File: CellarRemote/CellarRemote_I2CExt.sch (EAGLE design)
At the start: 14 parts, among them M1 BSS84, U1 P82B715D

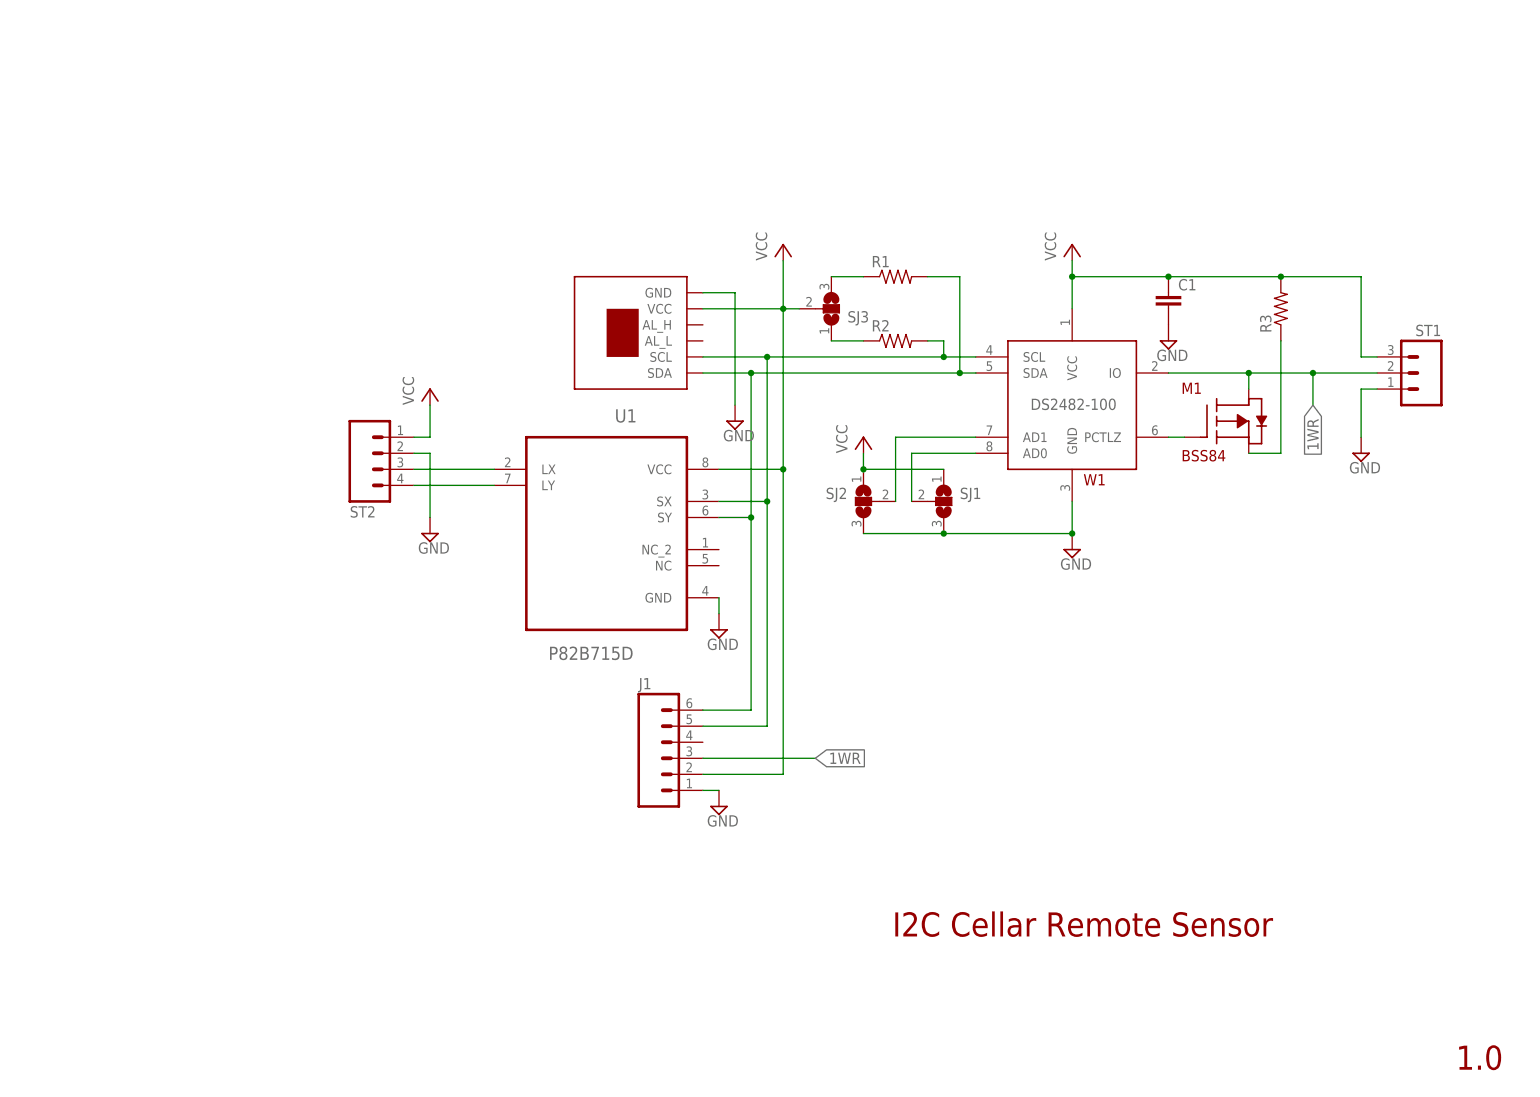
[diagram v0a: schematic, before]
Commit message: Added Raspberry pi board, updated I2C extender pullup resistors to other boards
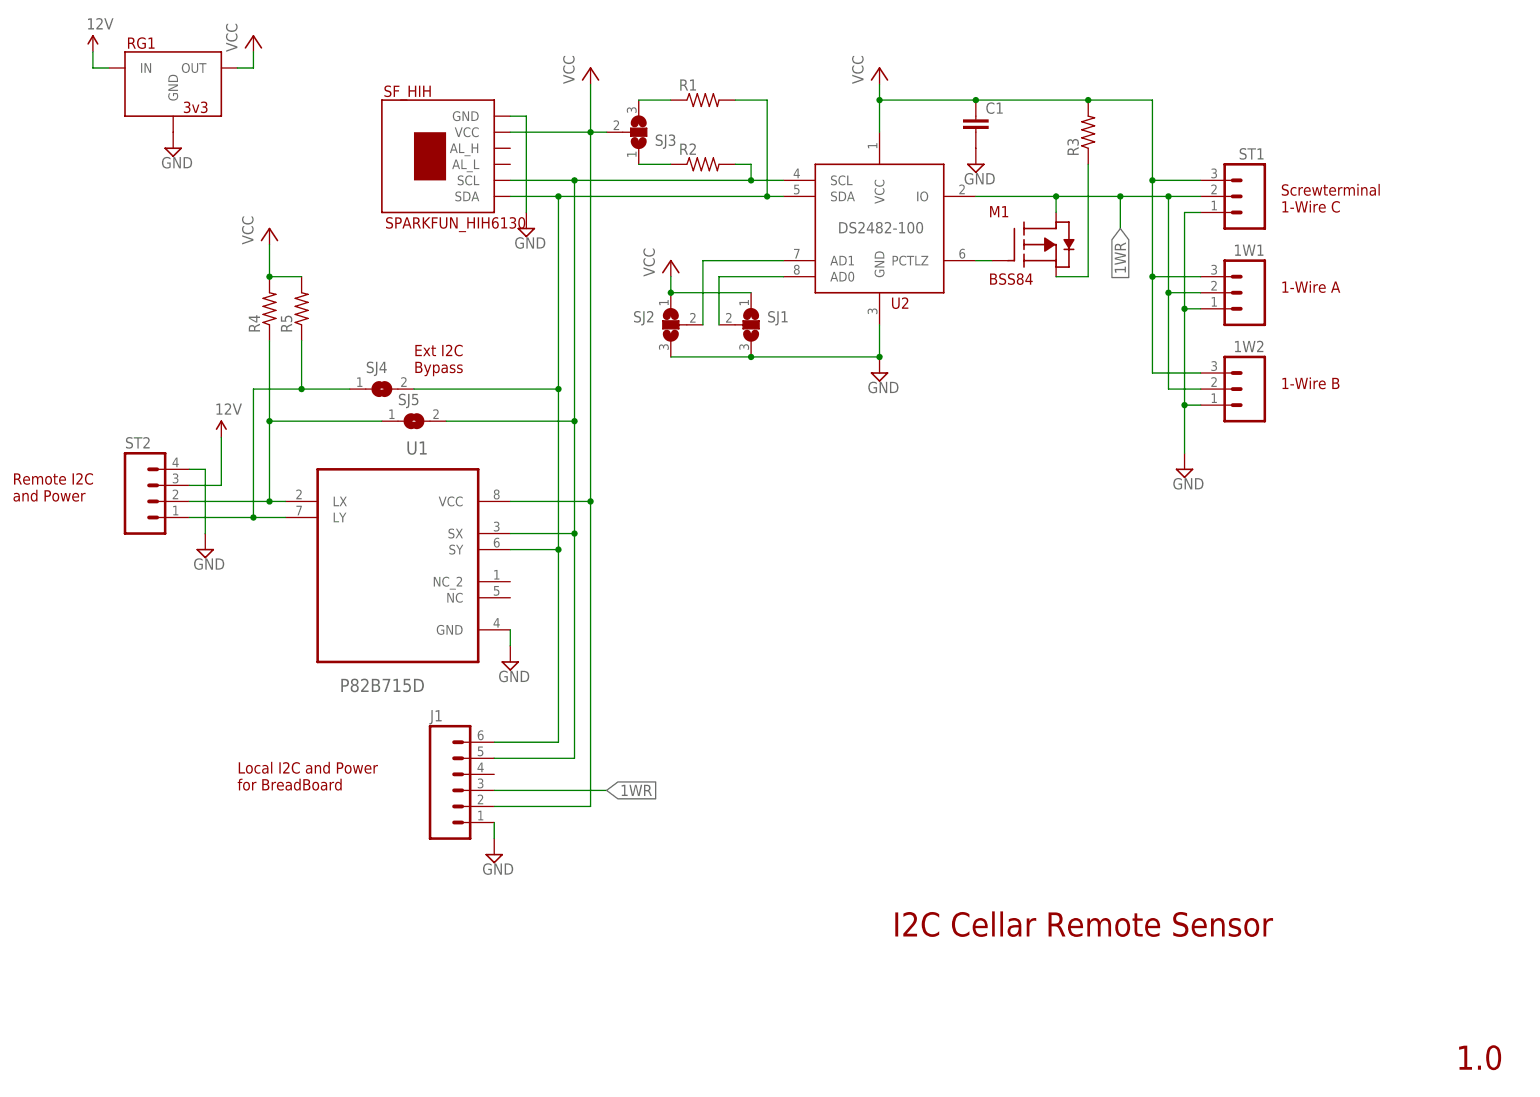
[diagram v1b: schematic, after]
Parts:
- removed W1: DS2482-100, PuffinOneWIre:DS2482-100
- added 1W1, 1W2: (no value), SparkFun-Connectors:M03PTH
- added R4, R5: (no value), SparkFun-Resistors:RESISTOR0805-RES
- added RG1: 3v3, Puffin:MURATA_REG
- added SJ4, SJ5: (no value), jumper:SJ
- added U2: DS2482-100, PuffinOneWIre:DS2482-100
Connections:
- new net 12V: RG1.IN, ST2.3
- net 1WR: now also 1W1.2, 1W2.2, U2.IO; no longer W1.IO
- net AD0: now also U2.AD0; no longer W1.AD0
- net AD1: now also U2.AD1; no longer W1.AD1
- net GND: now also 1W1.1, 1W2.1, RG1.GND, ST2.4, U2.GND; no longer ST2.2, W1.GND
- net N$1: now also U2.PCTLZ; no longer W1.PCTLZ
- net N$4: now also R4.1, SJ5.1, ST2.2; no longer ST2.3
- net N$5: now also R5.1, SJ4.1, ST2.1; no longer ST2.4
- net SCL: now also SJ5.2, U2.SCL; no longer W1.SCL
- net SDA: now also SJ4.2, U2.SDA; no longer W1.SDA
- net VCC: now also 1W1.3, 1W2.3, R4.2, R5.2, RG1.OUT, U2.VCC; no longer ST2.1, W1.VCC
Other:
- note added: "1-Wire A"
- note added: "1-Wire B"
- note added: "Ext I2C Bypass"
- note added: "Local I2C and Power for BreadBoard"
- note added: "Remote I2C and Power"
- note added: "Screwterminal 1-Wire C"
- moved on the sheet: C1, J1, M1, R1, R2, R3, SJ1, SJ2, SJ3, ST1, ST2, U1

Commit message: Ver 2 of CellarRemote with I2C extender
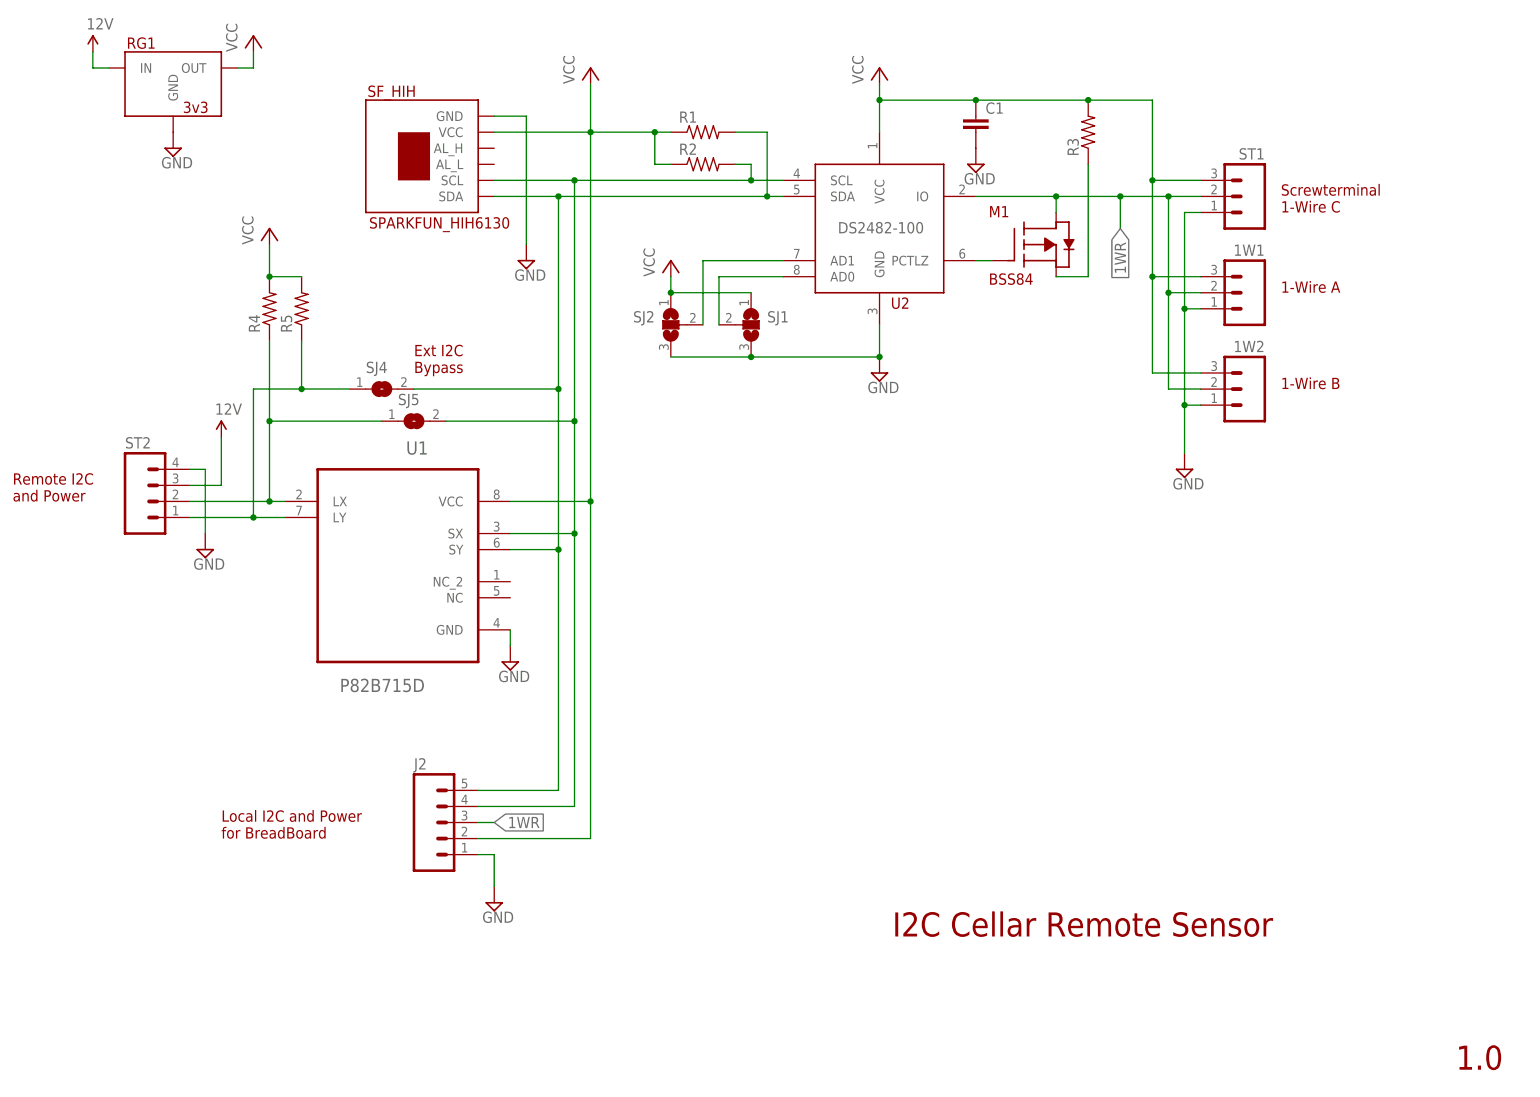
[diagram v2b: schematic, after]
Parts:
- removed J1: (no value), SparkFun-Connectors:M06SILK_FEMALE_PTH
- removed SJ3: (no value), jumper:SJ2W
- added J2: (no value), SparkFun-Connectors:M05PTH
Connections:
- removed net N$2: R1.1, SJ3.3
- removed net N$3: R2.1, SJ3.1
- net 1WR: now also J2.3; no longer J1.3
- net GND: now also J2.1; no longer J1.1
- net SCL: now also J2.4; no longer J1.5
- net SDA: now also J2.5; no longer J1.6
- net VCC: now also J2.2, R1.1, R2.1; no longer J1.2, SJ3.2
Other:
- moved on the sheet: R1, SF_HIH
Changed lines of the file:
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@@
 <part name="FRAME1" library="frames" deviceset="LETTER_L" device=""/>
 <part name="M1" library="Puffin" deviceset="BSS84" device=""/>
-<part name="SJ3" library="jumper" deviceset="SJ2W" device=""/>
 <part name="SUPPLY2" library="supply2" deviceset="GND" device=""/>
 <part name="SUPPLY5" library="supply2" deviceset="GND" device=""/>
 <part name="SF_HIH" library="Puffin" deviceset="SPARKFUN_HIH6130" device=""/>
-<part name="J1" library="SparkFun-Connectors" deviceset="M06" device="SILK_FEMALE_PTH"/>
 <part name="ST1" library="Puffin" deviceset="SCREWTERM_3" device=""/>
 <part name="ST2" library="Puffin" deviceset="SCREWTERM_4" device=""/>
@@
 <part name="SUPPLY10" library="supply2" deviceset="GND" device=""/>
 <part name="P+2" library="supply1" deviceset="VCC" device=""/>
+<part name="J2" library="SparkFun-Connectors" deviceset="M05" device="PTH"/>
 </parts>
 <sheets>
@@
 <text x="-35.56" y="55.88" size="1.778" layer="94">Remote I2C
 and Power</text>
-<text x="0" y="10.16" size="1.778" layer="94">Local I2C and Power
+<text x="-2.54" y="2.54" size="1.778" layer="94">Local I2C and Power
 for BreadBoard</text>
 <text x="165.1" y="101.6" size="1.778" layer="94">Screwterminal
@@
 <instances>
 <instance part="SUPPLY3" gate="GND" x="149.86" y="60.96"/>
-<instance part="SUPPLY4" gate="GND" x="40.64" y="0"/>
+<instance part="SUPPLY4" gate="GND" x="40.64" y="-7.62"/>
 <instance part="P+1" gate="VCC" x="101.6" y="124.46"/>
 <instance part="P+3" gate="VCC" x="55.88" y="124.46"/>
 <instance part="C1" gate="G$1" x="116.84" y="114.3"/>
-<instance part="R1" gate="G$1" x="73.66" y="119.38"/>
+<instance part="R1" gate="G$1" x="73.66" y="114.3"/>
 <instance part="R2" gate="G$1" x="73.66" y="109.22"/>
 <instance part="U2" gate="G$1" x="101.6" y="99.06"/>
@@
 <instance part="FRAME1" gate="G$2" x="101.6" y="-40.64"/>
 <instance part="M1" gate="G$1" x="127" y="93.98"/>
-<instance part="SJ3" gate="G$1" x="63.5" y="114.3" rot="MR180"/>
-<instance part="SUPPLY2" gate="GND" x="45.72" y="99.06"/>
+<instance part="SUPPLY2" gate="GND" x="45.72" y="93.98"/>
 <instance part="SUPPLY5" gate="GND" x="43.18" y="30.48"/>
-<instance part="SF_HIH" gate="G$1" x="33.02" y="109.22"/>
-<instance part="J1" gate="G$1" x="35.56" y="10.16"/>
+<instance part="SF_HIH" gate="G$1" x="30.48" y="109.22"/>
 <instance part="ST1" gate="G$1" x="160.02" y="106.68" rot="MR0"/>
 <instance part="ST2" gate="G$1" x="-15.24" y="58.42"/>
@@
 <instance part="SUPPLY10" gate="GND" x="-10.16" y="111.76"/>
 <instance part="P+2" gate="VCC" x="2.54" y="129.54"/>
+<instance part="J2" gate="G$1" x="30.48" y="5.08"/>
 </instances>
 <busses>
@@
 <pinref part="P+3" gate="VCC" pin="VCC"/>
 <wire x1="55.88" y1="114.3" x2="55.88" y2="121.92" width="0.1524" layer="91"/>
-<pinref part="SJ3" gate="G$1" pin="2"/>
-<wire x1="58.42" y1="114.3" x2="55.88" y2="114.3" width="0.1524" layer="91"/>
 <junction x="55.88" y="114.3"/>
-<wire x1="43.18" y1="114.3" x2="55.88" y2="114.3" width="0.1524" layer="91"/>
+<wire x1="40.64" y1="114.3" x2="55.88" y2="114.3" width="0.1524" layer="91"/>
 <pinref part="SF_HIH" gate="G$1" pin="VCC"/>
-<pinref part="J1" gate="G$1" pin="2"/>
-<wire x1="40.64" y1="7.62" x2="55.88" y2="7.62" width="0.1524" layer="91"/>
-<wire x1="55.88" y1="7.62" x2="55.88" y2="55.88" width="0.1524" layer="91"/>
+<wire x1="55.88" y1="2.54" x2="55.88" y2="55.88" width="0.1524" layer="91"/>
 <pinref part="U1" gate="A" pin="VCC"/>
 <wire x1="55.88" y1="55.88" x2="55.88" y2="114.3" width="0.1524" layer="91"/>
 <wire x1="43.18" y1="55.88" x2="55.88" y2="55.88" width="0.1524" layer="91"/>
 <junction x="55.88" y="55.88"/>
+<pinref part="J2" gate="G$1" pin="2"/>
+<wire x1="38.1" y1="2.54" x2="55.88" y2="2.54" width="0.1524" layer="91"/>
+<pinref part="R1" gate="G$1" pin="1"/>
+<wire x1="68.58" y1="114.3" x2="66.04" y2="114.3" width="0.1524" layer="91"/>
+<pinref part="R2" gate="G$1" pin="1"/>
+<wire x1="66.04" y1="114.3" x2="55.88" y2="114.3" width="0.1524" layer="91"/>
+<wire x1="68.58" y1="109.22" x2="66.04" y2="109.22" width="0.1524" layer="91"/>
+<wire x1="66.04" y1="109.22" x2="66.04" y2="114.3" width="0.1524" layer="91"/>
+<junction x="66.04" y="114.3"/>
 </segment>
 <segment>
@@
 </segment>
 <segment>
-<pinref part="SUPPLY4" gate="GND" pin="GND"/>
-<pinref part="J1" gate="G$1" pin="1"/>
-<wire x1="40.64" y1="5.08" x2="40.64" y2="2.54" width="0.1524" layer="91"/>
-</segment>
-<segment>
 <pinref part="SUPPLY3" gate="GND" pin="GND"/>
 <wire x1="152.4" y1="101.6" x2="149.86" y2="101.6" width="0.1524" layer="91"/>
@@
 <segment>
 <pinref part="SUPPLY2" gate="GND" pin="GND"/>
-<wire x1="43.18" y1="116.84" x2="45.72" y2="116.84" width="0.1524" layer="91"/>
-<wire x1="45.72" y1="116.84" x2="45.72" y2="101.6" width="0.1524" layer="91"/>
+<wire x1="40.64" y1="116.84" x2="45.72" y2="116.84" width="0.1524" layer="91"/>
+<wire x1="45.72" y1="116.84" x2="45.72" y2="96.52" width="0.1524" layer="91"/>
 <pinref part="SF_HIH" gate="G$1" pin="GND"/>
 </segment>
@@
 <pinref part="RG1" gate="RG$1" pin="GND"/>
 <pinref part="SUPPLY10" gate="GND" pin="GND"/>
+</segment>
+<segment>
+<pinref part="J2" gate="G$1" pin="1"/>
+<pinref part="SUPPLY4" gate="GND" pin="GND"/>
+<wire x1="38.1" y1="0" x2="40.64" y2="0" width="0.1524" layer="91"/>
+<wire x1="40.64" y1="0" x2="40.64" y2="-5.08" width="0.1524" layer="91"/>
 </segment>
 </net>
@@
 <junction x="81.28" y="106.68"/>
 <junction x="53.34" y="106.68"/>
-<wire x1="53.34" y1="15.24" x2="53.34" y2="50.8" width="0.1524" layer="91"/>
+<wire x1="53.34" y1="7.62" x2="53.34" y2="50.8" width="0.1524" layer="91"/>
 <wire x1="53.34" y1="50.8" x2="53.34" y2="68.58" width="0.1524" layer="91"/>
 <wire x1="53.34" y1="68.58" x2="53.34" y2="106.68" width="0.1524" layer="91"/>
-<wire x1="53.34" y1="106.68" x2="43.18" y2="106.68" width="0.1524" layer="91"/>
+<wire x1="53.34" y1="106.68" x2="40.64" y2="106.68" width="0.1524" layer="91"/>
 <pinref part="SF_HIH" gate="G$1" pin="SCL"/>
-<pinref part="J1" gate="G$1" pin="5"/>
-<wire x1="40.64" y1="15.24" x2="53.34" y2="15.24" width="0.1524" layer="91"/>
 <pinref part="U1" gate="A" pin="SX"/>
 <wire x1="43.18" y1="50.8" x2="53.34" y2="50.8" width="0.1524" layer="91"/>
@@
 <wire x1="33.02" y1="68.58" x2="53.34" y2="68.58" width="0.1524" layer="91"/>
 <junction x="53.34" y="68.58"/>
+<pinref part="J2" gate="G$1" pin="4"/>
+<wire x1="38.1" y1="7.62" x2="53.34" y2="7.62" width="0.1524" layer="91"/>
 </segment>
 </net>
@@
 <pinref part="R1" gate="G$1" pin="2"/>
 <wire x1="83.82" y1="104.14" x2="50.8" y2="104.14" width="0.1524" layer="91"/>
-<wire x1="78.74" y1="119.38" x2="83.82" y2="119.38" width="0.1524" layer="91"/>
-<wire x1="83.82" y1="119.38" x2="83.82" y2="104.14" width="0.1524" layer="91"/>
+<wire x1="78.74" y1="114.3" x2="83.82" y2="114.3" width="0.1524" layer="91"/>
+<wire x1="83.82" y1="114.3" x2="83.82" y2="104.14" width="0.1524" layer="91"/>
 <junction x="83.82" y="104.14"/>
-<wire x1="50.8" y1="17.78" x2="50.8" y2="48.26" width="0.1524" layer="91"/>
+<wire x1="50.8" y1="10.16" x2="50.8" y2="48.26" width="0.1524" layer="91"/>
 <junction x="50.8" y="104.14"/>
 <wire x1="50.8" y1="48.26" x2="50.8" y2="73.66" width="0.1524" layer="91"/>
 <wire x1="50.8" y1="73.66" x2="50.8" y2="104.14" width="0.1524" layer="91"/>
-<wire x1="50.8" y1="104.14" x2="43.18" y2="104.14" width="0.1524" layer="91"/>
+<wire x1="50.8" y1="104.14" x2="40.64" y2="104.14" width="0.1524" layer="91"/>
 <pinref part="SF_HIH" gate="G$1" pin="SDA"/>
-<pinref part="J1" gate="G$1" pin="6"/>
-<wire x1="40.64" y1="17.78" x2="50.8" y2="17.78" width="0.1524" layer="91"/>
 <pinref part="U1" gate="A" pin="SY"/>
 <wire x1="43.18" y1="48.26" x2="50.8" y2="48.26" width="0.1524" layer="91"/>
@@
 <wire x1="27.94" y1="73.66" x2="50.8" y2="73.66" width="0.1524" layer="91"/>
 <junction x="50.8" y="73.66"/>
+<pinref part="J2" gate="G$1" pin="5"/>
+<wire x1="38.1" y1="10.16" x2="50.8" y2="10.16" width="0.1524" layer="91"/>
 </segment>
 </net>
@@
 </segment>
 <segment>
-<label x="58.42" y="10.16" size="1.778" layer="95" xref="yes"/>
-<pinref part="J1" gate="G$1" pin="3"/>
-<wire x1="40.64" y1="10.16" x2="58.42" y2="10.16" width="0.1524" layer="91"/>
+<pinref part="J2" gate="G$1" pin="3"/>
+<wire x1="38.1" y1="5.08" x2="40.64" y2="5.08" width="0.1524" layer="91"/>
+<label x="40.64" y="5.08" size="1.778" layer="95" xref="yes"/>
 </segment>
 </net>
@@
 </segment>
 </net>
-<net name="N$2" class="0">
-<segment>
-<pinref part="R1" gate="G$1" pin="1"/>
-<pinref part="SJ3" gate="G$1" pin="3"/>
-<wire x1="68.58" y1="119.38" x2="63.5" y2="119.38" width="0.1524" layer="91"/>
-</segment>
-</net>
-<net name="N$3" class="0">
-<segment>
-<pinref part="R2" gate="G$1" pin="1"/>
-<pinref part="SJ3" gate="G$1" pin="1"/>
-<wire x1="68.58" y1="109.22" x2="63.5" y2="109.22" width="0.1524" layer="91"/>
-</segment>
-</net>
